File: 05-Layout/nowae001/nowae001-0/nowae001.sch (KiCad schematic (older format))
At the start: 25 parts, among them P1 USB_A_90, P2 CONN_4X1, Q1 IRLML6402, U1 FT230XQ, U2 TPS62152

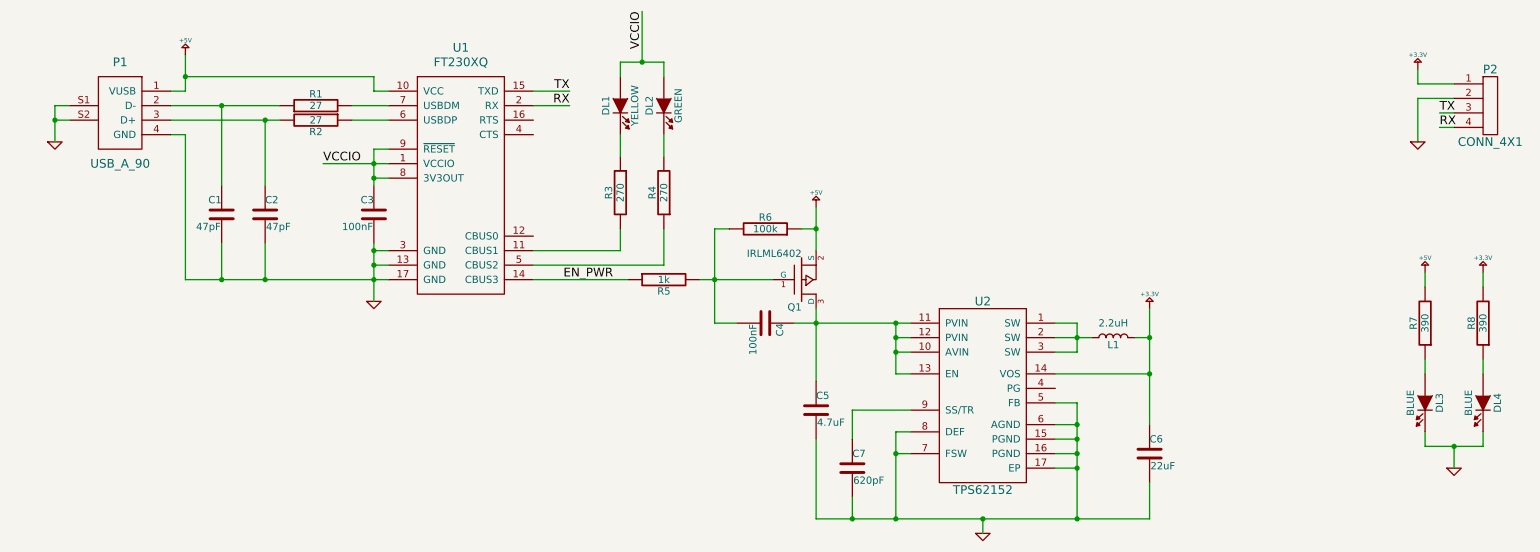
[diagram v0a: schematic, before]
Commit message: Updated components association in nowae001
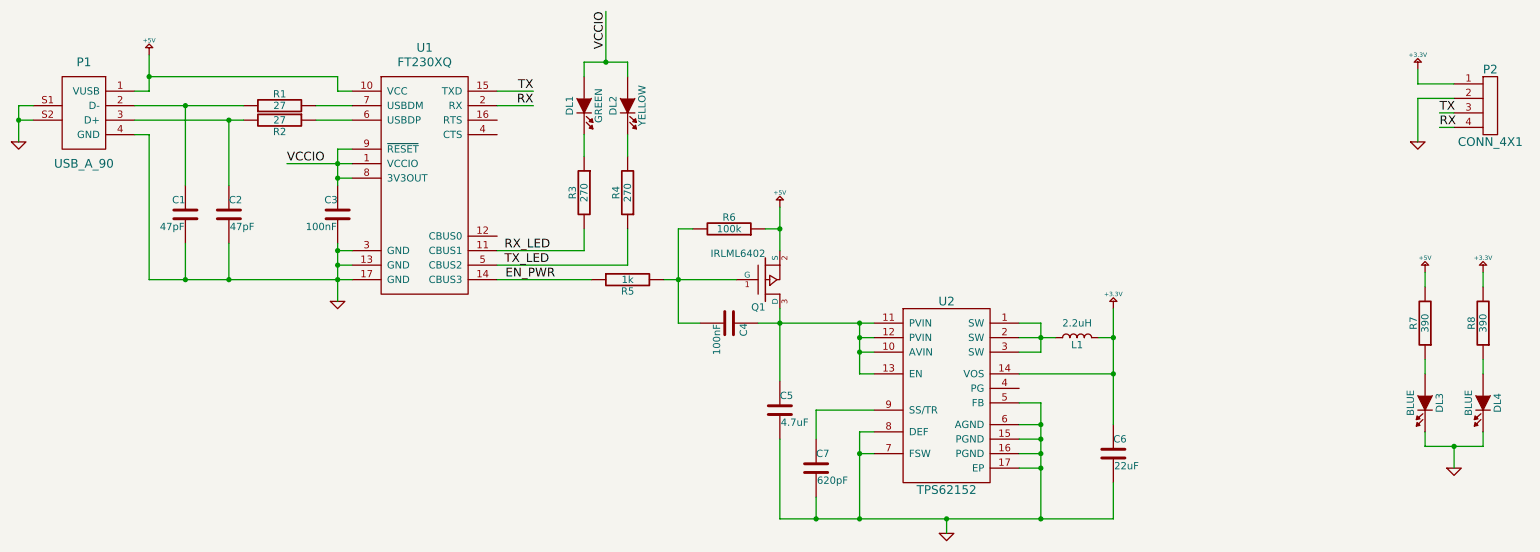
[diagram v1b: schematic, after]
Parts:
- U1: footprint QFN:QFN16_3x3_0.5_16+1 -> QFN:QFN16_4x4_0.65_16+1
- renumbered DL2 to DL1, DL1 to DL2
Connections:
- net RX_LED: now reaches R3.2, U1.11 (CBUS1)
- net TX_LED: now reaches R4.1, U1.5 (CBUS2)
- net at DL1.2 (K): now also R3.1; no longer R4.2
- net at DL2.2 (K): now also R4.2; no longer R3.1
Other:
- moved on the sheet: C1, C2, C3, C4, C5, C6, C7, DL1, DL2, L1, P1, Q1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
